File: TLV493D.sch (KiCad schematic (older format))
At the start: 7 parts, among them J1 Conn_01x04_Female, U1 TLV493D

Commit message: add hole M2, add logos and resize edge
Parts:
- R3: footprint Resistors_SMD:R_0805_HandSoldering -> Resistor_SMD:R_0805_2012Metric_Pad1.15x1.40mm_HandSolder
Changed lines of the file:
@@
 EESchema Schematic File Version 4
 LIBS:TLV493D-cache
-EELAYER 29 0
+EELAYER 30 0
 EELAYER END
 $Descr A4 11693 8268
@@
 F 0 "R3" H 2859 1876 50  0000 L CNN
 F 1 "1K2" H 2859 1785 50  0000 L CNN
-F 2 "Resistors_SMD:R_0805_HandSoldering" H 2800 1830 50  0001 C CNN
+F 2 "Resistor_SMD:R_0805_2012Metric_Pad1.15x1.40mm_HandSolder" H 2800 1830 50  0001 C CNN
 F 3 "~" H 2800 1830 50  0001 C CNN
 	1    2800 1830

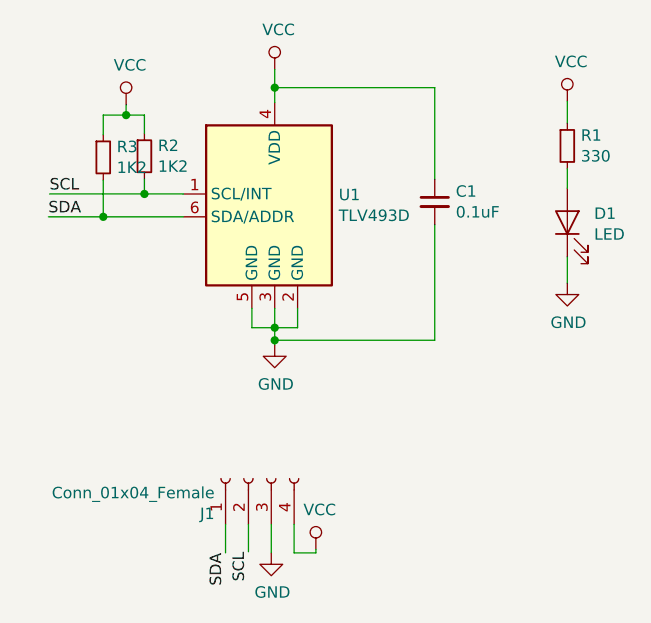
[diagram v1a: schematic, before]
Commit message: Change R1,R2,R3 and add footprint  manf
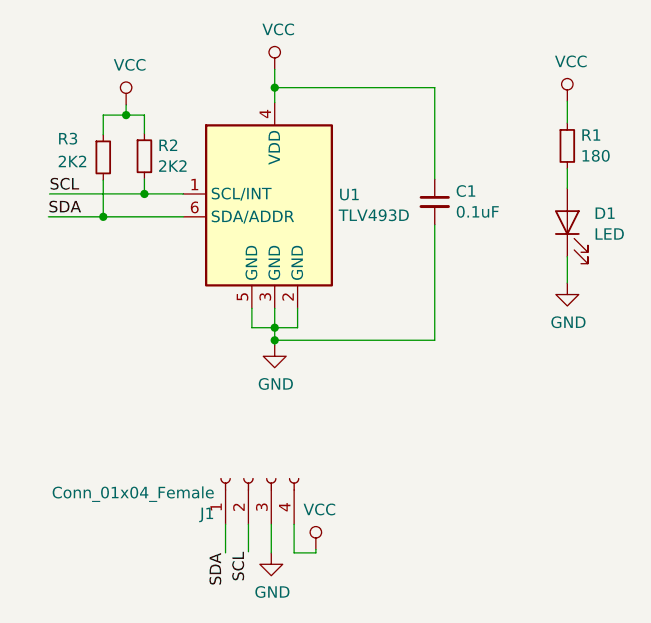
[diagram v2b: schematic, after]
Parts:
- C1: footprint Capacitors_SMD:C_0805_HandSoldering -> LED_SMD:LED_0805_2012Metric_Pad1.15x1.40mm_HandSolder; manf# (none) -> 885012207072
- D1: footprint LEDs:LED_0805_HandSoldering -> LED_SMD:LED_0805_2012Metric_Pad1.15x1.40mm_HandSolder; manf# (none) -> 150080RS75000
- R1: value 330 -> 180; footprint Resistors_SMD:R_0805_HandSoldering -> Resistor_SMD:R_0805_2012Metric_Pad1.15x1.40mm_HandSolder; manf# (none) -> RMCF0805JT180R
- R2: value 1K2 -> 2K2; footprint Resistors_SMD:R_0805_HandSoldering -> Resistor_SMD:R_0805_2012Metric_Pad1.15x1.40mm_HandSolder; manf# (none) -> RCG08052K20JNEA
- R3: value 1K2 -> 2K2; manf# (none) -> RCG08052K20JNEA
- U1: footprint Housings_SSOP:TSOP-6_1.65x3.05mm_Pitch0.95mm -> Package_SO:TSOP-6_1.65x3.05mm_P0.95mm; manf# (none) -> TLV493DA1B6HTSA2
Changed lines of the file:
@@
 Sheet 1 1
 Title "TLV493D"
-Date "2019-08-26"
+Date "2019-09-09"
 Rev "0.1v"
 Comp "Electronic Cats"
 Comment1 ""
 Comment2 ""
-Comment3 ""
+Comment3 "Montserrat Figueroa"
 Comment4 "Andres Sabas"
 $EndDescr
@@
 F 0 "U1" H 3830 2186 50  0000 L CNN
 F 1 "TLV493D" H 3830 2095 50  0000 L CNN
-F 2 "Housings_SSOP:TSOP-6_1.65x3.05mm_Pitch0.95mm" H 3500 1590 50  0001 C CNN
+F 2 "Package_SO:TSOP-6_1.65x3.05mm_P0.95mm" H 3500 1590 50  0001 C CNN
 F 3 "http://www.infineon.com/dgdl/Infineon-TLV493D-A1B6-DS-v01_00-EN.pdf?fileId=5546d462525dbac40152a6b85c760e80" H 3400 2590 50  0001 C CNN
+F 4 "TLV493DA1B6HTSA2" H 3550 2090 50  0001 C CNN "manf#"
 	1    3550 2090
 	1    0    0    -1
@@
 P 2980 1825
 F 0 "R2" H 3039 1871 50  0000 L CNN
-F 1 "1K2" H 3039 1780 50  0000 L CNN
-F 2 "Resistors_SMD:R_0805_HandSoldering" H 2980 1825 50  0001 C CNN
+F 1 "2K2" H 3039 1780 50  0000 L CNN
+F 2 "Resistor_SMD:R_0805_2012Metric_Pad1.15x1.40mm_HandSolder" H 2980 1825 50  0001 C CNN
 F 3 "~" H 2980 1825 50  0001 C CNN
+F 4 "RCG08052K20JNEA" H 2980 1825 50  0001 C CNN "manf#"
 	1    2980 1825
 	1    0    0    -1
@@
 U 1 1 5D64A83E
 P 2800 1830
-F 0 "R3" H 2859 1876 50  0000 L CNN
-F 1 "1K2" H 2859 1785 50  0000 L CNN
+F 0 "R3" H 2600 1910 50  0000 L CNN
+F 1 "2K2" H 2600 1810 50  0000 L CNN
 F 2 "Resistor_SMD:R_0805_2012Metric_Pad1.15x1.40mm_HandSolder" H 2800 1830 50  0001 C CNN
 F 3 "~" H 2800 1830 50  0001 C CNN
+F 4 "RCG08052K20JNEA" H 2800 1830 50  0001 C CNN "manf#"
 	1    2800 1830
 	1    0    0    -1
@@
 F 0 "C1" H 4342 2071 50  0000 L CNN
 F 1 "0.1uF" H 4342 1980 50  0000 L CNN
-F 2 "Capacitors_SMD:C_0805_HandSoldering" H 4250 2025 50  0001 C CNN
+F 2 "LED_SMD:LED_0805_2012Metric_Pad1.15x1.40mm_HandSolder" H 4250 2025 50  0001 C CNN
 F 3 "~" H 4250 2025 50  0001 C CNN
+F 4 "885012207072" H 4250 2025 50  0001 C CNN "manf#"
 	1    4250 2025
 	1    0    0    -1
@@
 P 4830 1780
 F 0 "R1" H 4889 1826 50  0000 L CNN
-F 1 "330" H 4889 1735 50  0000 L CNN
-F 2 "Resistors_SMD:R_0805_HandSoldering" H 4830 1780 50  0001 C CNN
+F 1 "180" H 4889 1735 50  0000 L CNN
+F 2 "Resistor_SMD:R_0805_2012Metric_Pad1.15x1.40mm_HandSolder" H 4830 1780 50  0001 C CNN
 F 3 "~" H 4830 1780 50  0001 C CNN
+F 4 "RMCF0805JT180R" H 4830 1780 50  0001 C CNN "manf#"
 	1    4830 1780
 	1    0    0    -1
@@
 F 0 "D1" V 4869 1998 50  0000 R CNN
 F 1 "LED" V 4778 1998 50  0000 R CNN
-F 2 "LEDs:LED_0805_HandSoldering" H 4830 2115 50  0001 C CNN
+F 2 "LED_SMD:LED_0805_2012Metric_Pad1.15x1.40mm_HandSolder" H 4830 2115 50  0001 C CNN
 F 3 "~" H 4830 2115 50  0001 C CNN
+F 4 "150080RS75000" H 4830 2115 50  0001 C CNN "manf#"
 	1    4830 2115
 	0    -1   -1   0

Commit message: Change capacitor footprint
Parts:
- C1: footprint LED_SMD:LED_0805_2012Metric_Pad1.15x1.40mm_HandSolder -> Capacitor_SMD:C_0805_2012Metric_Pad1.15x1.40mm_HandSolder
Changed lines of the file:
@@
 EESchema Schematic File Version 4
 LIBS:TLV493D-cache
-EELAYER 30 0
+EELAYER 29 0
 EELAYER END
 $Descr A4 11693 8268
@@
 F 0 "C1" H 4342 2071 50  0000 L CNN
 F 1 "0.1uF" H 4342 1980 50  0000 L CNN
-F 2 "LED_SMD:LED_0805_2012Metric_Pad1.15x1.40mm_HandSolder" H 4250 2025 50  0001 C CNN
+F 2 "Capacitor_SMD:C_0805_2012Metric_Pad1.15x1.40mm_HandSolder" H 4250 2025 50  0001 C CNN
 F 3 "~" H 4250 2025 50  0001 C CNN
 F 4 "885012207072" H 4250 2025 50  0001 C CNN "manf#"
